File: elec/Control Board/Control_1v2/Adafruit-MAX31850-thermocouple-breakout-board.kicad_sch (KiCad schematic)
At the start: 37 parts, among them J11 Screw_Terminal_01x02, J2 MAX31850K

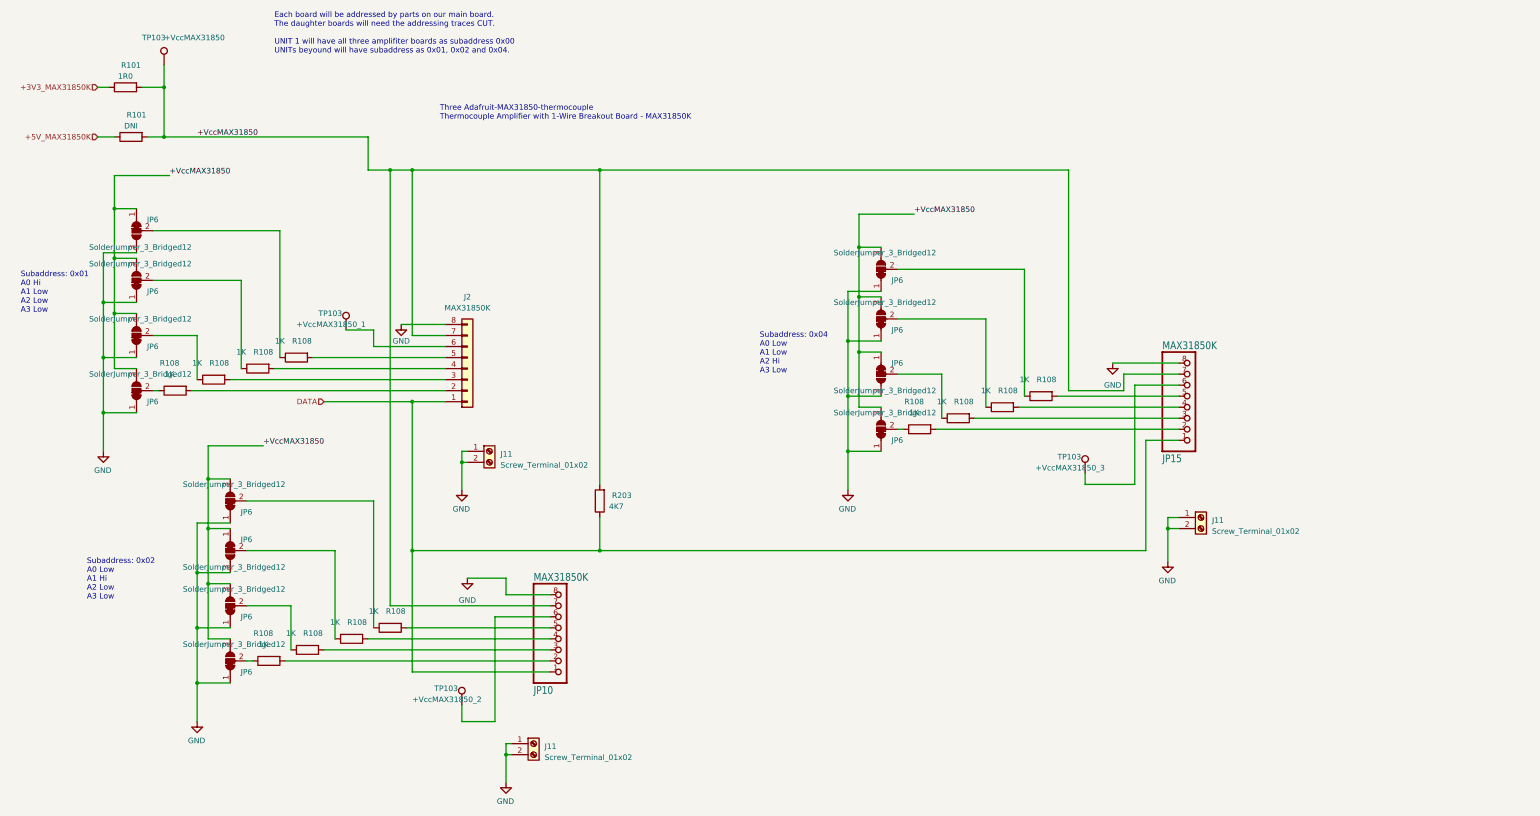
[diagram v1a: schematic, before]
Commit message: Contrl 1.2 schematic, fix for Issue Controller v1, COPI improperly attached to DO #54
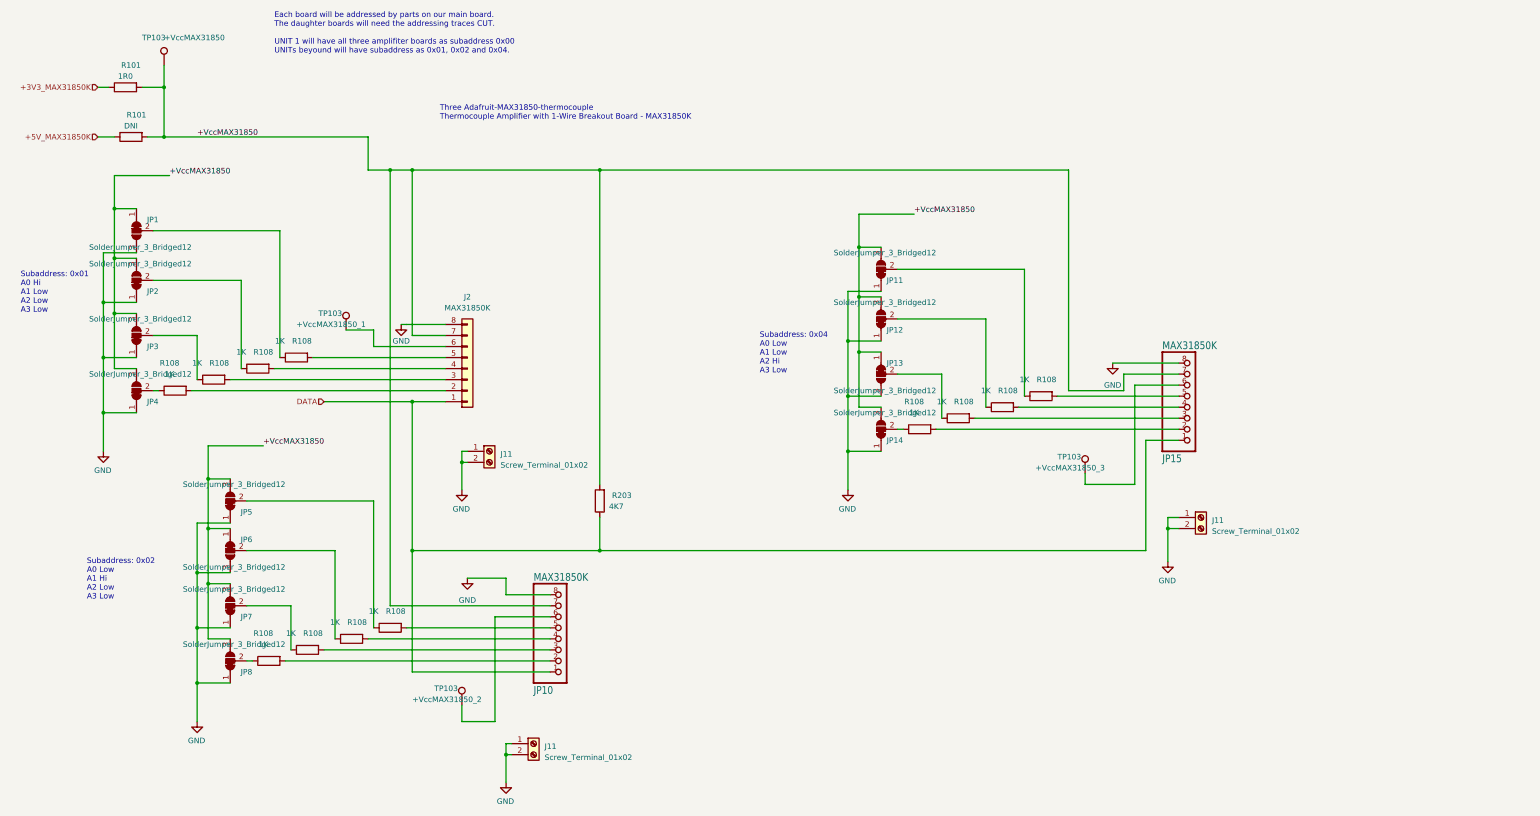
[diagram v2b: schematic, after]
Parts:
- renumbered JP6 to JP1, JP6 to JP11, JP6 to JP12, JP6 to JP13, JP6 to JP14, JP6 to JP2, JP6 to JP3, JP6 to JP4, JP6 to JP5, JP6 to JP7, JP6 to JP8
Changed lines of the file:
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@@
   (symbol (lib_id "Jumper:SolderJumper_3_Bridged12") (at 271.78 138.43 90) (mirror x) (unit 1)
     (in_bom yes) (on_board yes) (dnp no)
-    (property "Reference" "JP6" (at 276.86 135.89 90)
+    (property "Reference" "JP13" (at 276.86 135.89 90)
       (effects (font (size 1.27 1.27)) (justify left))
     )
@@
   (symbol (lib_id "Jumper:SolderJumper_3_Bridged12") (at 100.33 142.24 90) (unit 1)
     (in_bom yes) (on_board yes) (dnp no)
-    (property "Reference" "JP6" (at 105.41 144.78 90)
+    (property "Reference" "JP4" (at 105.41 144.78 90)
       (effects (font (size 1.27 1.27)) (justify left))
     )
@@
   (symbol (lib_id "Jumper:SolderJumper_3_Bridged12") (at 100.33 116.84 90) (unit 1)
     (in_bom yes) (on_board yes) (dnp no)
-    (property "Reference" "JP6" (at 105.41 119.38 90)
+    (property "Reference" "JP2" (at 105.41 119.38 90)
       (effects (font (size 1.27 1.27)) (justify left))
     )
@@
   (symbol (lib_id "Jumper:SolderJumper_3_Bridged12") (at 121.92 167.64 90) (unit 1)
     (in_bom yes) (on_board yes) (dnp no)
-    (property "Reference" "JP6" (at 127 170.18 90)
+    (property "Reference" "JP5" (at 127 170.18 90)
       (effects (font (size 1.27 1.27)) (justify left))
     )
@@
   (symbol (lib_id "Jumper:SolderJumper_3_Bridged12") (at 271.78 125.73 90) (unit 1)
     (in_bom yes) (on_board yes) (dnp no)
-    (property "Reference" "JP6" (at 276.86 128.27 90)
+    (property "Reference" "JP12" (at 276.86 128.27 90)
       (effects (font (size 1.27 1.27)) (justify left))
     )
@@
   (symbol (lib_id "Jumper:SolderJumper_3_Bridged12") (at 100.33 105.41 90) (mirror x) (unit 1)
     (in_bom yes) (on_board yes) (dnp no)
-    (property "Reference" "JP6" (at 105.41 102.87 90)
+    (property "Reference" "JP1" (at 105.41 102.87 90)
       (effects (font (size 1.27 1.27)) (justify left))
     )
@@
   (symbol (lib_id "Jumper:SolderJumper_3_Bridged12") (at 271.78 114.3 90) (unit 1)
     (in_bom yes) (on_board yes) (dnp no)
-    (property "Reference" "JP6" (at 276.86 116.84 90)
+    (property "Reference" "JP11" (at 276.86 116.84 90)
       (effects (font (size 1.27 1.27)) (justify left))
     )
@@
   (symbol (lib_id "Jumper:SolderJumper_3_Bridged12") (at 100.33 129.54 90) (unit 1)
     (in_bom yes) (on_board yes) (dnp no)
-    (property "Reference" "JP6" (at 105.41 132.08 90)
+    (property "Reference" "JP3" (at 105.41 132.08 90)
       (effects (font (size 1.27 1.27)) (justify left))
     )
@@
   (symbol (lib_id "Jumper:SolderJumper_3_Bridged12") (at 121.92 191.77 90) (unit 1)
     (in_bom yes) (on_board yes) (dnp no)
-    (property "Reference" "JP6" (at 127 194.31 90)
+    (property "Reference" "JP7" (at 127 194.31 90)
       (effects (font (size 1.27 1.27)) (justify left))
     )
@@
   (symbol (lib_id "Jumper:SolderJumper_3_Bridged12") (at 271.78 151.13 90) (unit 1)
     (in_bom yes) (on_board yes) (dnp no)
-    (property "Reference" "JP6" (at 276.86 153.67 90)
+    (property "Reference" "JP14" (at 276.86 153.67 90)
       (effects (font (size 1.27 1.27)) (justify left))
     )
@@
   (symbol (lib_id "Jumper:SolderJumper_3_Bridged12") (at 121.92 204.47 90) (unit 1)
     (in_bom yes) (on_board yes) (dnp no)
-    (property "Reference" "JP6" (at 127 207.01 90)
-      (effects (font (size 1.27 1.27)) (justify left))
-    )
+    (property "Reference" "JP8" (at 127 207.01 90)
+      (effects (font (size 1.27 1.27)) (justify left))
+    )

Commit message: Contrl 1.2 schematic, adding to schematic a forth thermocouple amp.
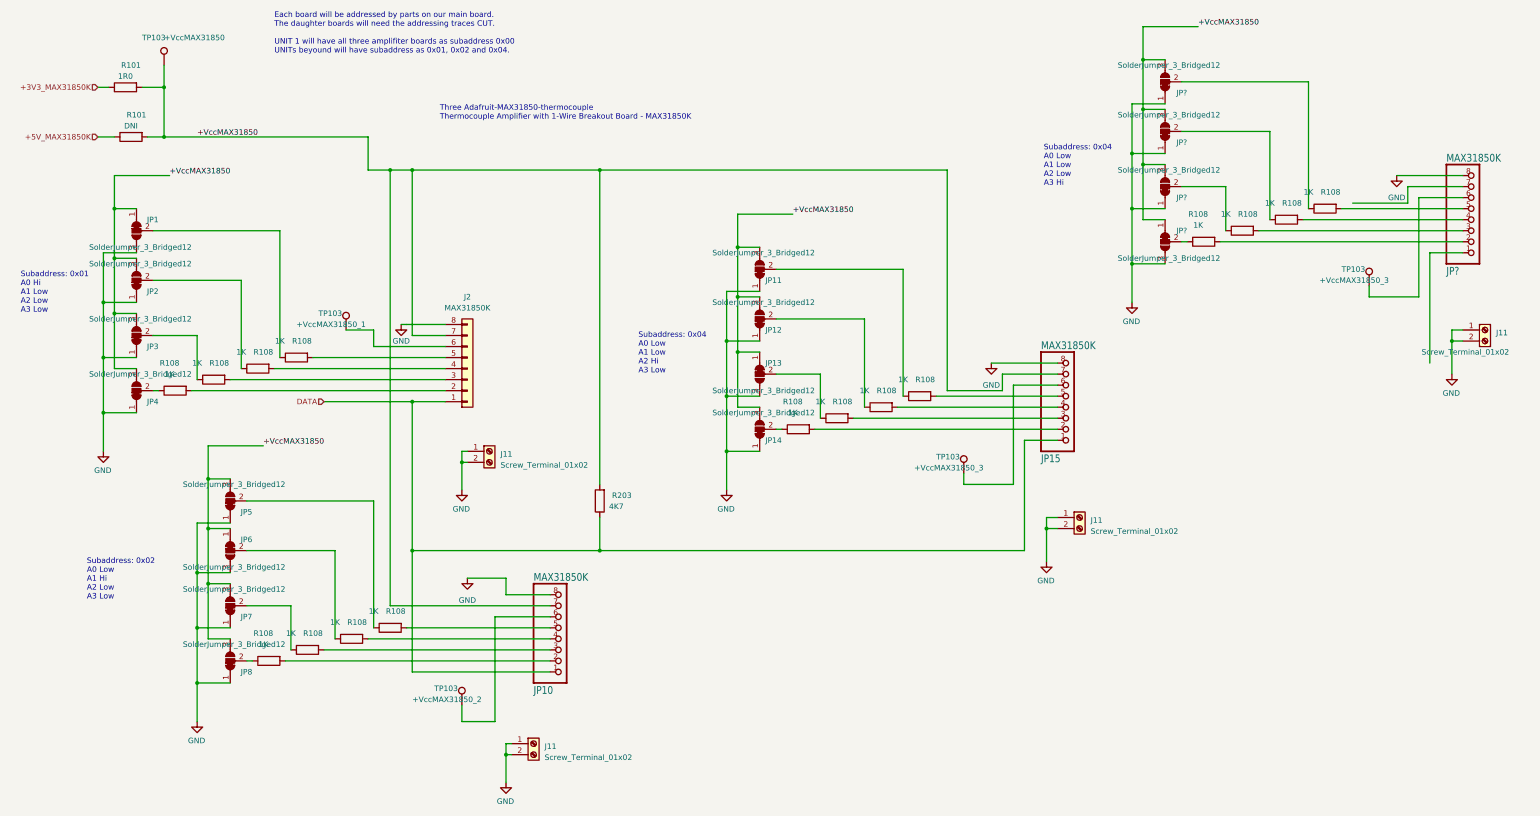
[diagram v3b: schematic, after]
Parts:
- added J11: Screw_Terminal_01x02, TerminalBlock_TE-Connectivity:TerminalBlock_TE_282834-2_1x02_P2.54mm_Horizontal, symbol Connector:Screw_Terminal_01x02
- added JP?: MAX31850K, PubInv_KiCad_PCB:Adafruit_MAX31850K_Module, symbol Control v1-eagle-import:microbuilder_HEADER-1X870MIL
- added JP? (x4): SolderJumper_3_Bridged12, Jumper:SolderJumper-3_P1.3mm_Bridged12_RoundedPad1.0x1.5mm, symbol Jumper:SolderJumper_3_Bridged12
- added R108 (x4): 1K, Resistor_SMD:R_0603_1608Metric_Pad0.98x0.95mm_HandSolder, symbol Device:R
- added TP103: +VccMAX31850_3, TestPoint:TestPoint_Loop_D2.54mm_Drill1.5mm_Beaded, symbol Connector:TestPoint
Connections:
- net +VccMAX31850: now also JP?.1 (A), JP?.3 (B), JP?.3 (B), JP?.3 (B)
- net GND: now also J11.1 (Pin_1), J11.2 (Pin_2), JP?.1 (A), JP?.1 (A), JP?.1 (A), JP?.3 (B), JP?.8
- new net: JP?.2 (C), R108.1 (x4)
- new net: JP?.3, R108.2
- new net: JP?.2, R108.2
- new net: JP?.4, R108.2
- new net: JP?.5, R108.2
- new net: JP?.6, TP103.1
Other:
- note added: "Subaddress: 0x04 A0 Low A1 Low A2 Low A3 Hi"
- moved on the sheet: J11, JP11, JP12, JP13, JP14, JP15, R108, TP103

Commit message: Update Control_1v2.kicad_sch for correct JLCPCB part number on JST 2 pin XH Connector. Wire up J30 as connector for OEDCS Fan.
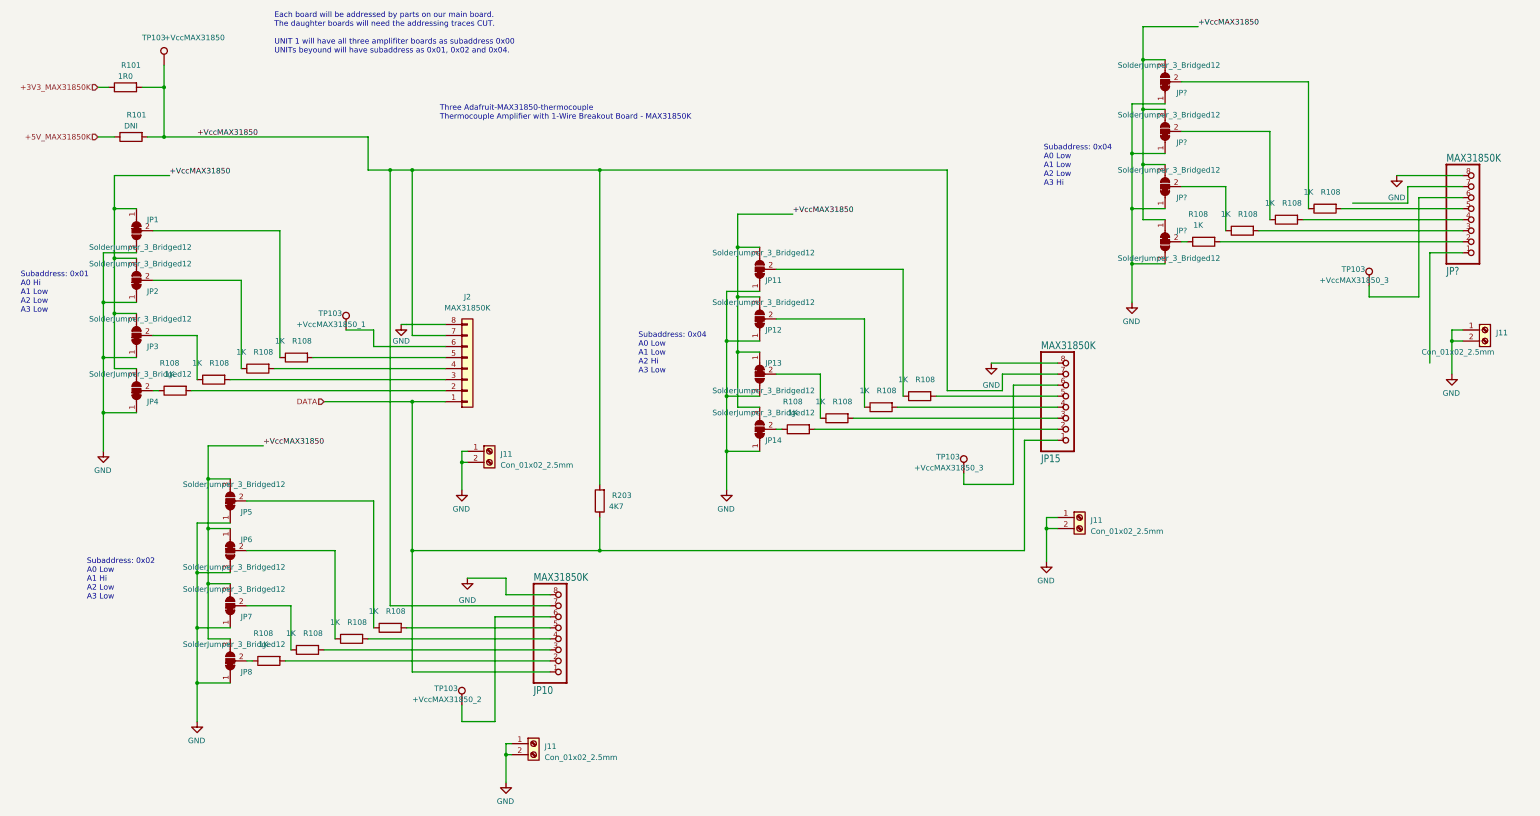
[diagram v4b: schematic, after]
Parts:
- J11: value Screw_Terminal_01x02 -> Con_01x02_2.5mm; footprint TerminalBlock_TE-Connectivity:TerminalBlock_TE_282834-2_1x02_P2.54mm_Horizontal -> Connector_JST:JST_XH_B2B-XH-AM_1x02_P2.50mm_Vertical; Cost 0.1537 -> 0.2156; MPN DB125-2.54-2P-GN-S -> B2B-XH-A-GU; Manufacturer DIBO -> JST
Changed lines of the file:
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@@
       (effects (font (size 1.27 1.27)) (justify left))
     )
-    (property "Value" "Screw_Terminal_01x02" (at 320.04 174.625 0)
-      (effects (font (size 1.27 1.27)) (justify left))
-    )
-    (property "Footprint" "TerminalBlock_TE-Connectivity:TerminalBlock_TE_282834-2_1x02_P2.54mm_Horizontal" (at 317.5 171.45 0)
+    (property "Value" "Con_01x02_2.5mm" (at 320.04 174.625 0)
+      (effects (font (size 1.27 1.27)) (justify left))
+    )
+    (property "Footprint" "Connector_JST:JST_XH_B2B-XH-AM_1x02_P2.50mm_Vertical" (at 317.5 171.45 0)
       (effects (font (size 1.27 1.27)) hide)
     )
@@
       (effects (font (size 1.27 1.27)) hide)
     )
-    (property "Cost" "0.1537" (at 317.5 171.45 0)
-      (effects (font (size 1.27 1.27)) hide)
-    )
-    (property "Description" "1x2P XH 1 2.5mm 2 Brass Plugin,P=2.5mm Wire To Board / Wire To Wire Connector ROHS" (at 317.5 171.45 0)
+    (property "Cost" "0.2156" (at 317.5 171.45 0)
+      (effects (font (size 1.27 1.27)) hide)
+    )
+    (property "Description" "1x2P 2P XH Gold 2 -25℃~+85℃ 3A 1 2.5mm Brass Direct Insert Plugin,P=2.5mm Wire To Board Connector ROHS" (at 317.5 171.45 0)
       (effects (font (size 1.27 1.27)) hide)
     )
@@
       (effects (font (size 1.27 1.27)) hide)
     )
-    (property "MPN" "DB125-2.54-2P-GN-S" (at 317.5 171.45 0)
-      (effects (font (size 1.27 1.27)) hide)
-    )
-    (property "Manufacturer" "DIBO" (at 317.5 171.45 0)
+    (property "MPN" "B2B-XH-A-GU" (at 317.5 171.45 0)
+      (effects (font (size 1.27 1.27)) hide)
+    )
+    (property "Manufacturer" "JST" (at 317.5 171.45 0)
       (effects (font (size 1.27 1.27)) hide)
     )
@@
       (effects (font (size 1.27 1.27)) (justify left))
     )
-    (property "Value" "Screw_Terminal_01x02" (at 194.31 226.695 0)
-      (effects (font (size 1.27 1.27)) (justify left))
-    )
-    (property "Footprint" "TerminalBlock_TE-Connectivity:TerminalBlock_TE_282834-2_1x02_P2.54mm_Horizontal" (at 191.77 223.52 0)
+    (property "Value" "Con_01x02_2.5mm" (at 194.31 226.695 0)
+      (effects (font (size 1.27 1.27)) (justify left))
+    )
+    (property "Footprint" "Connector_JST:JST_XH_B2B-XH-AM_1x02_P2.50mm_Vertical" (at 191.77 223.52 0)
       (effects (font (size 1.27 1.27)) hide)
     )
@@
       (effects (font (size 1.27 1.27)) hide)
     )
-    (property "Cost" "0.1537" (at 191.77 223.52 0)
-      (effects (font (size 1.27 1.27)) hide)
-    )
-    (property "Description" "1x2P XH 1 2.5mm 2 Brass Plugin,P=2.5mm Wire To Board / Wire To Wire Connector ROHS" (at 191.77 223.52 0)
+    (property "Cost" "0.2156" (at 191.77 223.52 0)
+      (effects (font (size 1.27 1.27)) hide)
+    )
+    (property "Description" "1x2P 2P XH Gold 2 -25℃~+85℃ 3A 1 2.5mm Brass Direct Insert Plugin,P=2.5mm Wire To Board Connector ROHS" (at 191.77 223.52 0)
       (effects (font (size 1.27 1.27)) hide)
     )
@@
       (effects (font (size 1.27 1.27)) hide)
     )
-    (property "MPN" "DB125-2.54-2P-GN-S" (at 191.77 223.52 0)
-      (effects (font (size 1.27 1.27)) hide)
-    )
-    (property "Manufacturer" "DIBO" (at 191.77 223.52 0)
+    (property "MPN" "B2B-XH-A-GU" (at 191.77 223.52 0)
+      (effects (font (size 1.27 1.27)) hide)
+    )
+    (property "Manufacturer" "JST" (at 191.77 223.52 0)
       (effects (font (size 1.27 1.27)) hide)
     )
@@
       (effects (font (size 1.27 1.27)) (justify left))
     )
-    (property "Value" "Screw_Terminal_01x02" (at 184.15 159.385 0)
-      (effects (font (size 1.27 1.27)) (justify left))
-    )
-    (property "Footprint" "TerminalBlock_TE-Connectivity:TerminalBlock_TE_282834-2_1x02_P2.54mm_Horizontal" (at 181.61 156.21 0)
+    (property "Value" "Con_01x02_2.5mm" (at 184.15 159.385 0)
+      (effects (font (size 1.27 1.27)) (justify left))
+    )
+    (property "Footprint" "Connector_JST:JST_XH_B2B-XH-AM_1x02_P2.50mm_Vertical" (at 181.61 156.21 0)
       (effects (font (size 1.27 1.27)) hide)
     )
@@
       (effects (font (size 1.27 1.27)) hide)
     )
-    (property "Cost" "0.1537" (at 181.61 156.21 0)
-      (effects (font (size 1.27 1.27)) hide)
-    )
-    (property "Description" "1x2P XH 1 2.5mm 2 Brass Plugin,P=2.5mm Wire To Board / Wire To Wire Connector ROHS" (at 181.61 156.21 0)
+    (property "Cost" "0.2156" (at 181.61 156.21 0)
+      (effects (font (size 1.27 1.27)) hide)
+    )
+    (property "Description" "1x2P 2P XH Gold 2 -25℃~+85℃ 3A 1 2.5mm Brass Direct Insert Plugin,P=2.5mm Wire To Board Connector ROHS" (at 181.61 156.21 0)
       (effects (font (size 1.27 1.27)) hide)
     )
@@
       (effects (font (size 1.27 1.27)) hide)
     )
-    (property "MPN" "DB125-2.54-2P-GN-S" (at 181.61 156.21 0)
-      (effects (font (size 1.27 1.27)) hide)
-    )
-    (property "Manufacturer" "DIBO" (at 181.61 156.21 0)
+    (property "MPN" "B2B-XH-A-GU" (at 181.61 156.21 0)
+      (effects (font (size 1.27 1.27)) hide)
+    )
+    (property "Manufacturer" "JST" (at 181.61 156.21 0)
       (effects (font (size 1.27 1.27)) hide)
     )
@@
       (effects (font (size 1.27 1.27)) (justify left))
     )
-    (property "Value" "Screw_Terminal_01x02" (at 396.24 133.35 0)
-      (effects (font (size 1.27 1.27)) (justify left))
-    )
-    (property "Footprint" "TerminalBlock_TE-Connectivity:TerminalBlock_TE_282834-2_1x02_P2.54mm_Horizontal" (at 410.845 128.27 0)
+    (property "Value" "Con_01x02_2.5mm" (at 396.24 133.35 0)
+      (effects (font (size 1.27 1.27)) (justify left))
+    )
+    (property "Footprint" "Connector_JST:JST_XH_B2B-XH-AM_1x02_P2.50mm_Vertical" (at 410.845 128.27 0)
       (effects (font (size 1.27 1.27)) hide)
     )
@@
       (effects (font (size 1.27 1.27)) hide)
     )
-    (property "Cost" "0.1537" (at 410.845 128.27 0)
-      (effects (font (size 1.27 1.27)) hide)
-    )
-    (property "Description" "1x2P XH 1 2.5mm 2 Brass Plugin,P=2.5mm Wire To Board / Wire To Wire Connector ROHS" (at 410.845 128.27 0)
+    (property "Cost" "0.2156" (at 410.845 128.27 0)
+      (effects (font (size 1.27 1.27)) hide)
+    )
+    (property "Description" "1x2P 2P XH Gold 2 -25℃~+85℃ 3A 1 2.5mm Brass Direct Insert Plugin,P=2.5mm Wire To Board Connector ROHS" (at 410.845 128.27 0)
       (effects (font (size 1.27 1.27)) hide)
     )
@@
       (effects (font (size 1.27 1.27)) hide)
     )
-    (property "MPN" "DB125-2.54-2P-GN-S" (at 410.845 128.27 0)
-      (effects (font (size 1.27 1.27)) hide)
-    )
-    (property "Manufacturer" "DIBO" (at 410.845 128.27 0)
-      (effects (font (size 1.27 1.27)) hide)
-    )
+    (property "MPN" "B2B-XH-A-GU" (at 410.845 128.27 0)
+      (effects (font (size 1.27 1.27)) hide)
+    )
+    (property "Manufacturer" "JST" (at 410.845 128.27 0)
+      (effects (font (size 1.27 1.27)) hide)
+    )
